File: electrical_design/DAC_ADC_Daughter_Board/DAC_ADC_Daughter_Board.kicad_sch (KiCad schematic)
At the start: 10 parts, among them J1 External Pin Conn, J2 ADC_DAC_CONN, J3 I2C Conn, U1 ADC081C021CIMK_NOPB, U2 DAC5571IDBVR

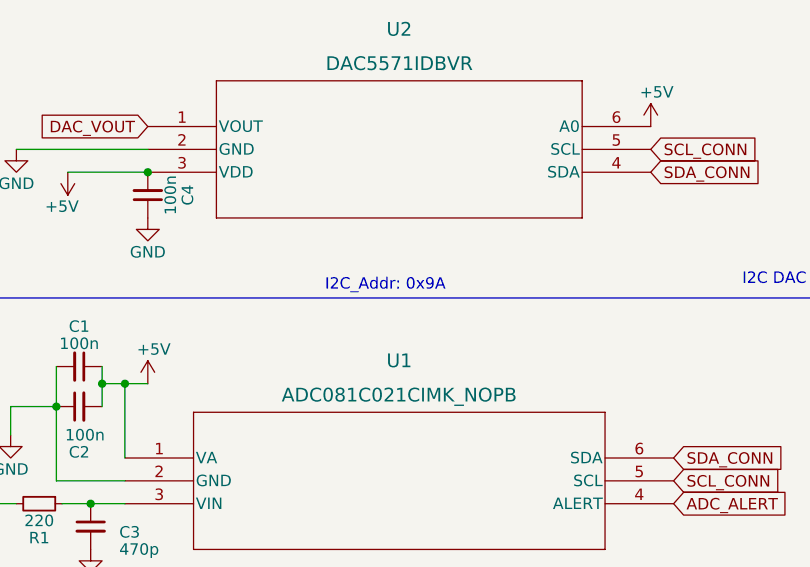
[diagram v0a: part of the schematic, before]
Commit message: change i2c address of DAC
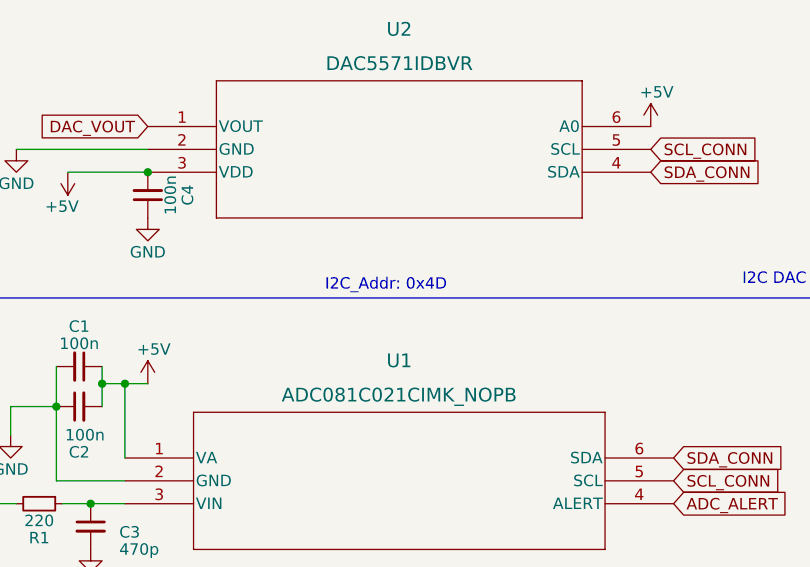
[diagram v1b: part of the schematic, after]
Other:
- note added: "I2C_Addr: 0x4D"
- note removed: "I2C_Addr: 0x9A"
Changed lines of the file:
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@@
     (effects (font (size 1.27 1.27)) (justify left bottom))
   )
-  (text "I2C_Addr: 0x9A" (at 144.78 115.57 0)
+  (text "I2C_Addr: 0x4D" (at 144.78 115.57 0)
     (effects (font (size 1.27 1.27)) (justify left bottom))
   )
